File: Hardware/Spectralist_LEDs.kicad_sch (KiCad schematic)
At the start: 26 parts, among them U1 PCA9956B_LED_Driver

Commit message: Updates to LED board
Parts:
- added C1: 100nF, Capacitor_SMD:C_0603_1608Metric, symbol Device:C_Small
- added C2: 10uF, Capacitor_SMD:C_0805_2012Metric, symbol Device:C_Small
- added J1: Conn_01x03_Pin, Connector_PinHeader_2.54mm:PinHeader_1x03_P2.54mm_Vertical, symbol Connector:Conn_01x03_Pin
- added J2, J3: Conn_01x02_Pin, Connector_PinHeader_2.54mm:PinHeader_1x02_P2.54mm_Vertical, symbol Connector:Conn_01x02_Pin
- added R1, R3: 10k, Resistor_SMD:R_0603_1608Metric, symbol Device:R
- added R2: 2k, Resistor_SMD:R_0603_1608Metric, symbol Device:R
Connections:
- net GND: now also C1.1, C2.1, J1.2 (Pin_2), J2.2 (Pin_2), J3.2 (Pin_2), R2.1; no longer D1.1 (K), D10.1 (K), D11.1 (K), D12.1 (K), D13.1 (K), D14.1 (K), D15.1 (K), D16.1 (K), D17.1 (K), D18.1 (K), D19.1 (K), D2.1 (K), D20.1 (K), D21.1 (K), D22.1 (K), D23.1 (K), D24.1 (K), D3.1 (K), D4.1 (K), D5.1 (K), D6.1 (K), D7.1 (K), D8.1 (K), D9.1 (K)
- net at U1.20 (LED12): now also D13.1 (K); no longer D13.2 (A)
- net at U1.23 (LED14): now also D15.1 (K); no longer D15.2 (A)
- net at U1.10 (LED4): now also D5.1 (K); no longer D5.2 (A)
- net at U1.16 (LED9): now also D10.1 (K); no longer D10.2 (A)
- net at U1.11 (LED5): now also D6.1 (K); no longer D6.2 (A)
- net at U1.26 (LED16): now also D17.1 (K); no longer D17.2 (A)
- net at U1.13 (LED7): now also D8.1 (K); no longer D8.2 (A)
- net at U1.33 (LED23): now also D24.1 (K); no longer D24.2 (A)
- net at U1.24 (LED15): now also D16.1 (K); no longer D16.2 (A)
- net at U1.27 (LED17): now also D18.1 (K); no longer D18.2 (A)
- net at D25.2 (A): now also R1.2
- net at U1.30 (LED20): now also D21.1 (K); no longer D21.2 (A)
- net at U1.6 (LED0): now also D1.1 (K); no longer D1.2 (A)
- net at U1.22 (LED13): now also D14.1 (K); no longer D14.2 (A)
- net at U1.8 (LED2): now also D3.1 (K); no longer D3.2 (A)
- net at U1.19 (LED11): now also D12.1 (K); no longer D12.2 (A)
- net at U1.7 (LED1): now also D2.1 (K); no longer D2.2 (A)
- net at U1.9 (LED3): now also D4.1 (K); no longer D4.2 (A)
- net at U1.32 (LED22): now also D23.1 (K); no longer D23.2 (A)
- net at U1.15 (LED8): now also D9.1 (K); no longer D9.2 (A)
- net at U1.28 (LED18): now also D19.1 (K); no longer D19.2 (A)
- net at U1.1 (REXT): now also R2.2
- net at U1.12 (LED6): now also D7.1 (K); no longer D7.2 (A)
- net at U1.17 (LED10): now also D11.1 (K); no longer D11.2 (A)
- net at U1.29 (LED19): now also D20.1 (K); no longer D20.2 (A)
- net at U1.31 (LED21): now also D22.1 (K); no longer D22.2 (A)
- net at U1.35 (~{RESET}): now also R3.2
- net LED_SCL: now reaches U1.36 (SCL)
- net LED_SCL: now also J1.1 (Pin_1)
- net LED_SDA: now reaches U1.37 (SDA)
- net LED_SDA: now also J1.3 (Pin_3)
- net +3.3V: now reaches U1.38 (VDD)
- net +3.3V: now also C1.2, J3.1 (Pin_1), R3.1
- new net +12V: C2.2, D1.2 (A), D10.2 (A), D11.2 (A), D12.2 (A), D13.2 (A), D14.2 (A), D15.2 (A), D16.2 (A), D17.2 (A), D18.2 (A), D19.2 (A), D2.2 (A), D20.2 (A), D21.2 (A), D22.2 (A), D23.2 (A), D24.2 (A), D3.2 (A), D4.2 (A), D5.2 (A), D6.2 (A), D7.2 (A), D8.2 (A), D9.2 (A), J2.1 (Pin_1), R1.1
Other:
- moved on the sheet: D1, D10, D11, D12, D13, D14, D15, D16, D17, D18, D19, D2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

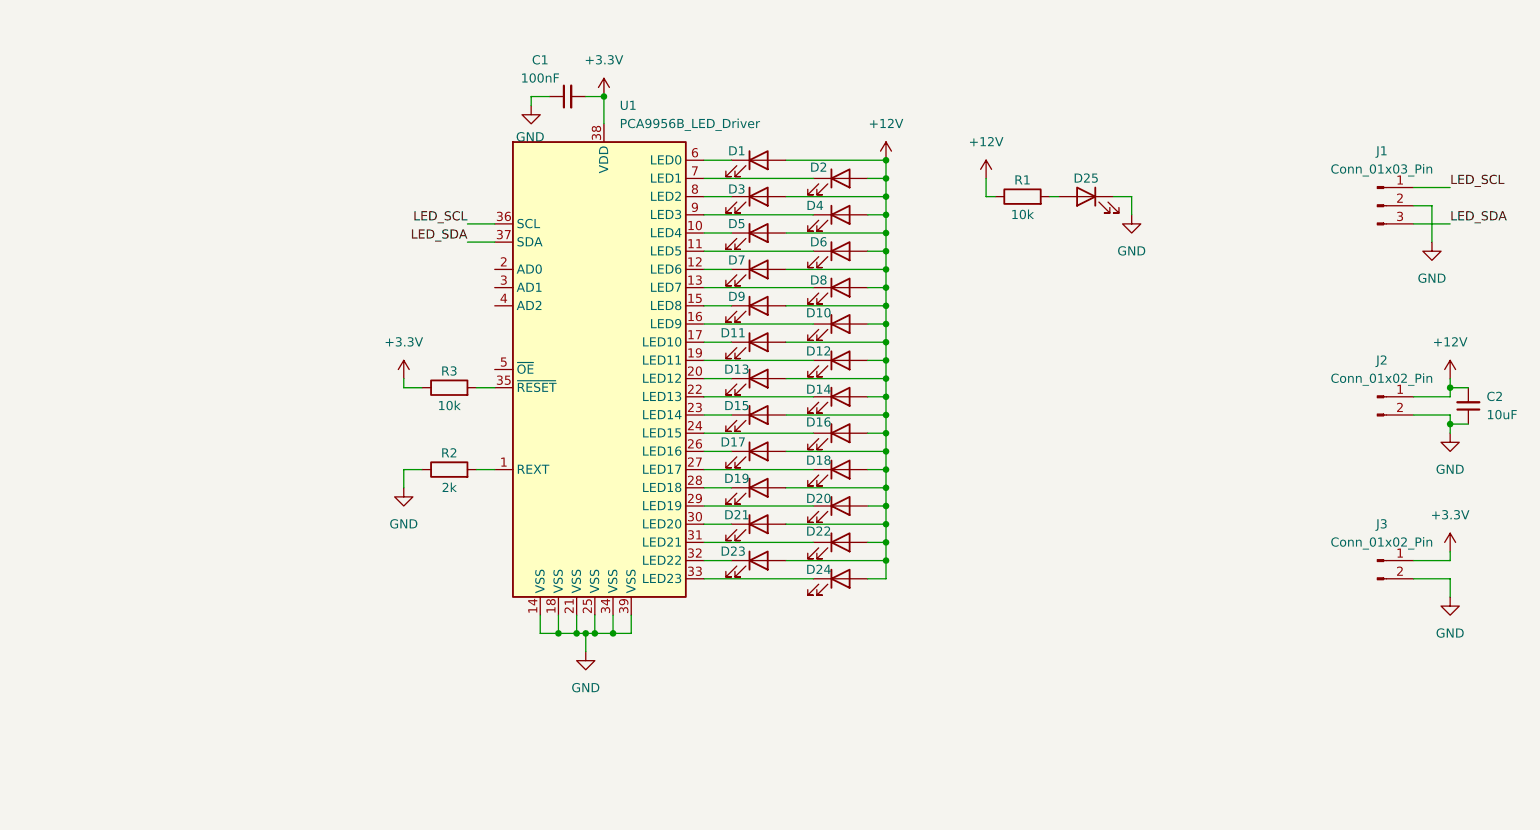
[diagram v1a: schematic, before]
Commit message: Curvy traces on LED board
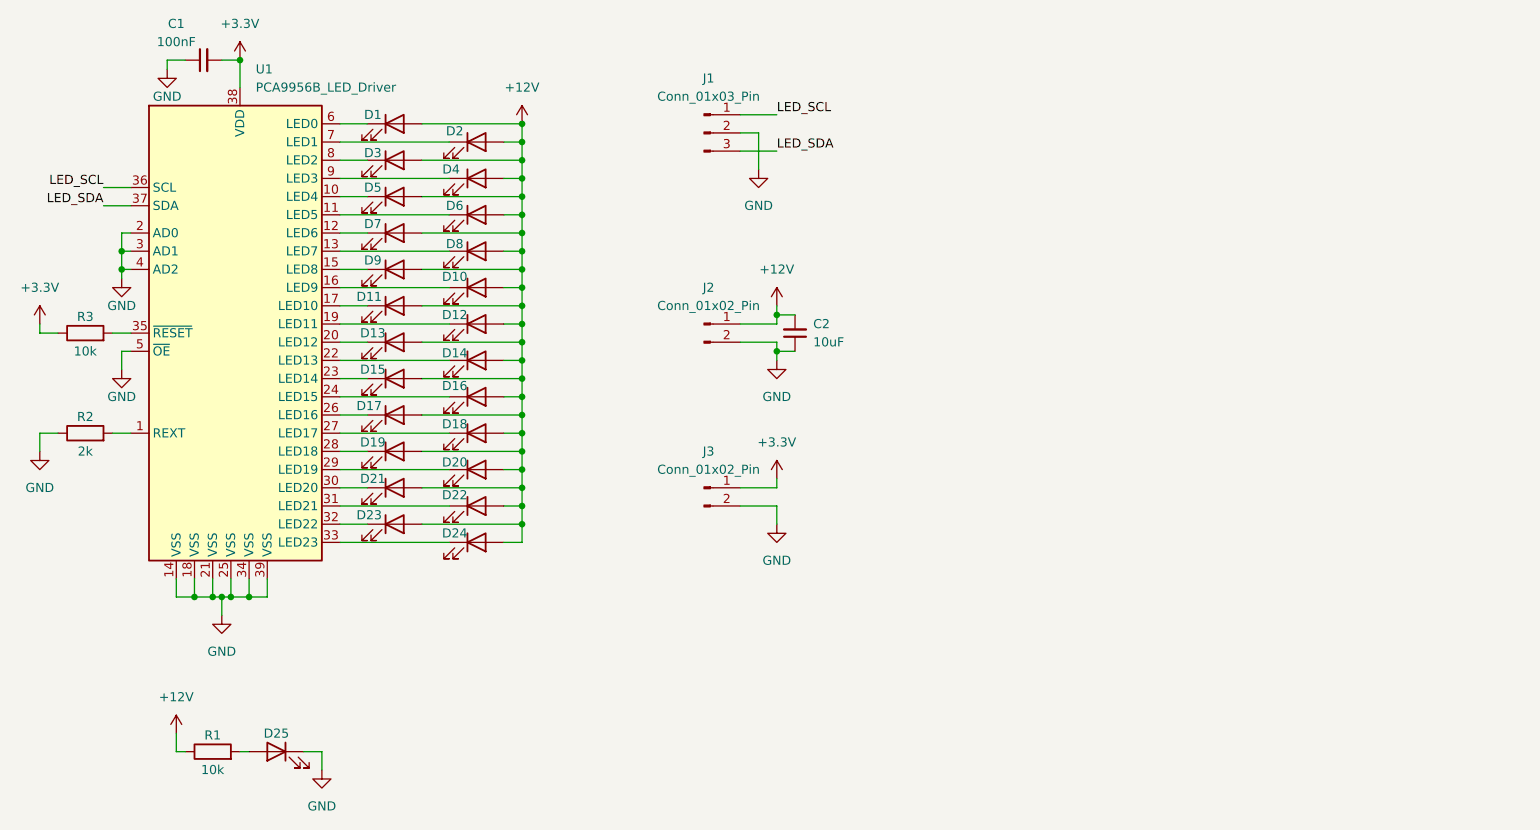
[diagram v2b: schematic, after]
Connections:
- net GND: now also U1.2 (AD0), U1.3 (AD1), U1.4 (AD2), U1.5 (~{OE})
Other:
- moved on the sheet: C1, C2, D1, D10, D11, D12, D13, D14, D15, D16, D17, D18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

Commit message: v1.0 PCBs sent to production
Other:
- company: (none) -> Mountjoy Modular
- title: (none) -> Spectralist LED board
- moved on the sheet: C1, D1, D10, D11, D12, D13, D14, D15, D16, D17, D18, D19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
